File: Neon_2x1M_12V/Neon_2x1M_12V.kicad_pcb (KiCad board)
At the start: 2 copper layers, 77.5 x 51.5 mm, 47 parts, among them J2 Barrel_Jack_MountingPin, J4 Barrel_Jack_MountingPin, J5 Barrel_Jack_MountingPin, J6 Conn_01x03_Pin, Q1 IRLML2502TRPBF, Q2 IRLML2502TRPBF, Q3 BSS138, Q4 BSS138, Q5 BSS138, SW1 SW_Push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

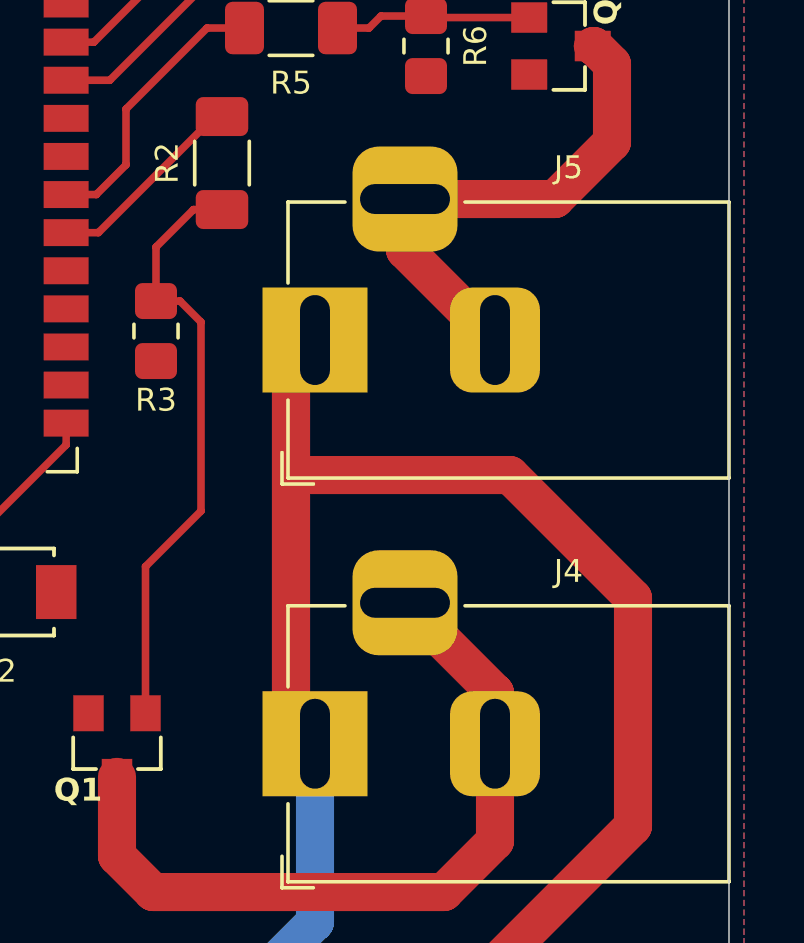
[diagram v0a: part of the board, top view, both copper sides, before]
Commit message: updated output jack routing
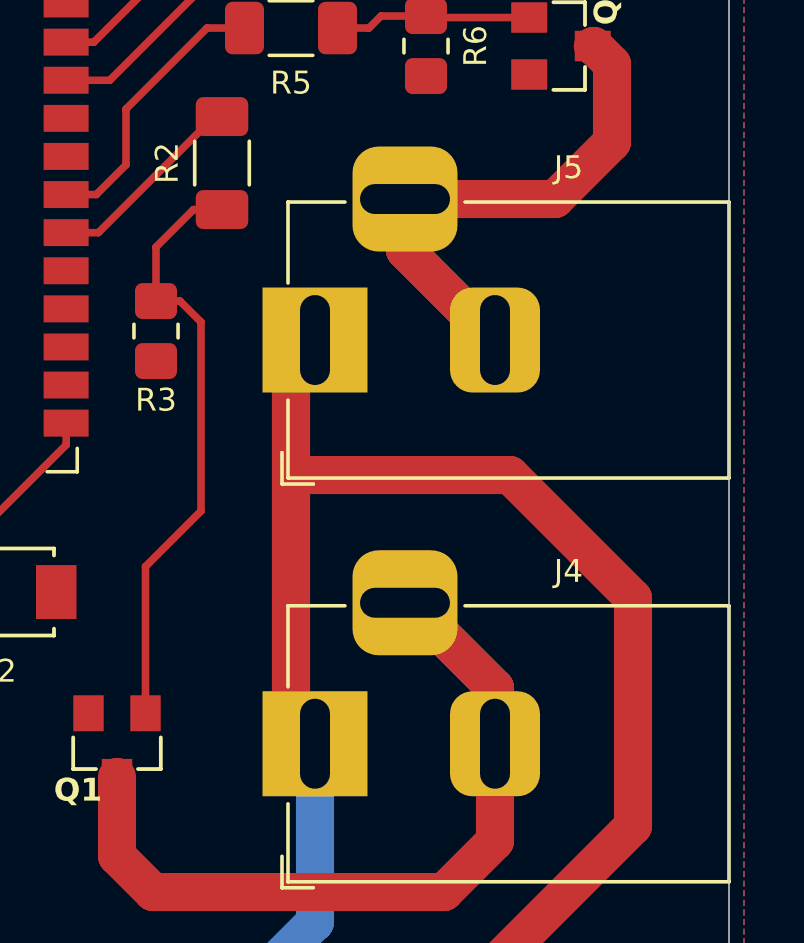
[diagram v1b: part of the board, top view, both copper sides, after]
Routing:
- net B_Jack: track 25.6 -> 31.8 mm
- net P_Jack: track 17.1 -> 23.1 mm
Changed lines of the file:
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@@
 	)
 	(segment
-		(start 167.3 69.7)
-		(end 166.1 68.5)
+		(start 178.7 64.7575)
+		(end 178.7 62.9)
 		(width 1.27)
 		(layer "F.Cu")
@@
 	)
 	(segment
-		(start 178.7 64.7575)
-		(end 178.7 63.0575)
+		(start 167.3 69.7)
+		(end 166.1 68.5)
 		(width 1.27)
 		(layer "F.Cu")
@@
 	)
 	(segment
-		(start 178.7 63.0575)
+		(start 178.7 62.9)
+		(end 175.8575 60.0575)
+		(width 1.27)
+		(layer "F.Cu")
+		(net 37)
+	)
+	(segment
+		(start 175.8575 60.0575)
 		(end 175.7 60.0575)
 		(width 1.27)
@@
 		(width 1.27)
 		(layer "F.Cu")
+		(net 37)
+	)
+	(segment
+		(start 175.8575 60.0575)
+		(end 178.7 62.9)
+		(width 1.27)
+		(layer "B.Cu")
+		(net 37)
+	)
+	(segment
+		(start 178.7 62.9)
+		(end 178.7 64.7575)
+		(width 1.27)
+		(layer "B.Cu")
+		(net 37)
+	)
+	(segment
+		(start 175.7 60.0575)
+		(end 175.8575 60.0575)
+		(width 1.27)
+		(layer "B.Cu")
 		(net 37)
 	)
@@
 		(net 38)
 	)
+	(segment
+		(start 175.7 46.6)
+		(end 175.7 48.3)
+		(width 1.27)
+		(layer "B.Cu")
+		(net 38)
+	)
+	(segment
+		(start 175.7 48.3)
+		(end 178.7 51.3)
+		(width 1.27)
+		(layer "B.Cu")
+		(net 38)
+	)

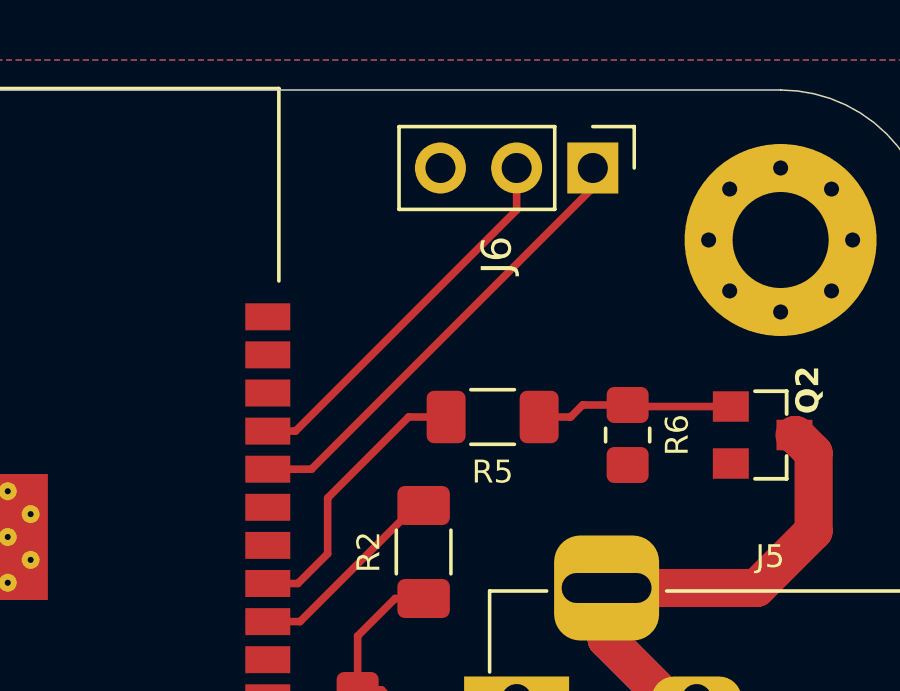
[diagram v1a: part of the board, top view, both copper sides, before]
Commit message: updated JST PIN header placement
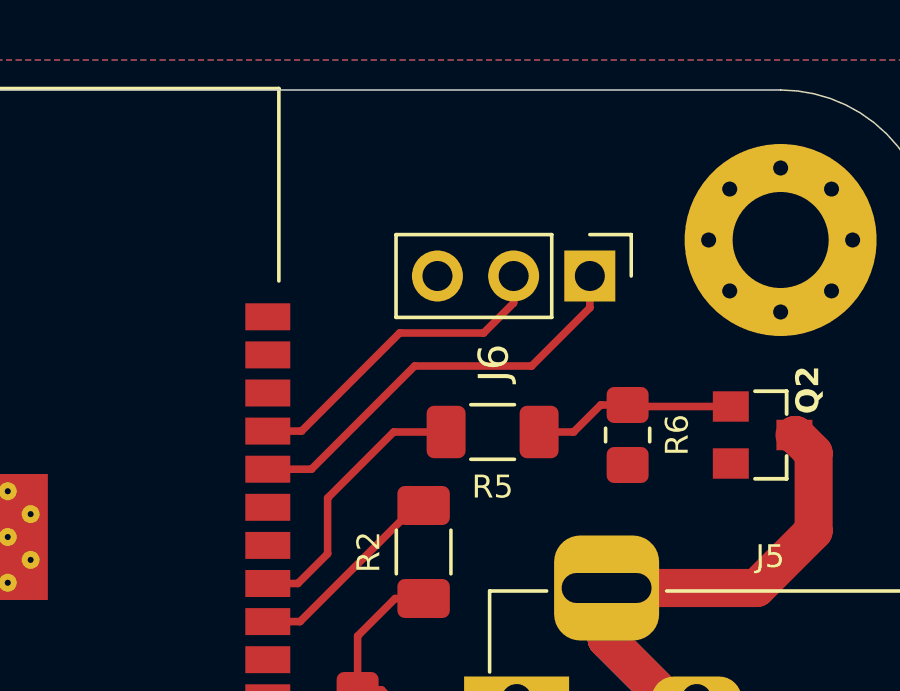
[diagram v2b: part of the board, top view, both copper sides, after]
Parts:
- moved J6 3.60 mm to (175.1, 36.2)
- moved R5 0.50 mm to (171.9, 41.4)
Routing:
- net ESP_U0TX: track 12.7 -> 10.9 mm
- net ESP_U0RX: track 15.4 -> 14.0 mm
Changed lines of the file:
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@@
 	(footprint "Connector_PinHeader_2.54mm:PinHeader_1x03_P2.54mm_Vertical"
 		(layer "F.Cu")
-		(at 175.24 32.6 -90)
+		(at 175.14 36.2 -90)
 		(descr "Through hole straight pin header, 1x03, 2.54mm pitch, single row")
 		(tags "Through hole pin header THT 1x03 2.54mm single row")
@@
 	(footprint "Resistor_SMD:R_1206_3216Metric_Pad1.30x1.75mm_HandSolder"
 		(layer "F.Cu")
-		(at 171.9 40.9 180)
+		(at 171.9 41.4 180)
 		(descr "Resistor SMD 1206 (3216 Metric), square (rectangular) end terminal, IPC-7351 nominal with elongated pad for handsoldering. (Body size source: IPC-SM-782 page 72, https://www.pcb-3d.com/wordpress/wp-content/uploads/ipc-sm-782a_amendment_1_and_2.pdf), generated with kicad-footprint-generator")
 		(tags "resistor handsolder")
@@
 	)
 	(segment
-		(start 165.33 41.37)
-		(end 164.405 41.37)
+		(start 171.6 38.1)
+		(end 172.6 37.1)
 		(width 0.254)
 		(layer "F.Cu")
@@
 	)
 	(segment
-		(start 172.7 32.6)
-		(end 172.7 34)
+		(start 168.8 38.1)
+		(end 171.6 38.1)
 		(width 0.254)
 		(layer "F.Cu")
@@
 	)
 	(segment
-		(start 172.7 34)
-		(end 165.33 41.37)
+		(start 172.6 37.1)
+		(end 172.6 36.2)
+		(width 0.254)
+		(layer "F.Cu")
+		(net 26)
+	)
+	(segment
+		(start 164.405 41.37)
+		(end 165.53 41.37)
+		(width 0.254)
+		(layer "F.Cu")
+		(net 26)
+	)
+	(segment
+		(start 165.53 41.37)
+		(end 168.8 38.1)
 		(width 0.254)
 		(layer "F.Cu")
@@
 	)
 	(segment
-		(start 164.405 46.45)
-		(end 165.409 46.45)
+		(start 166.4 45.459)
+		(end 166.4 43.6)
 		(width 0.254)
 		(layer "F.Cu")
@@
 	)
 	(segment
-		(start 165.409 46.45)
-		(end 166.4 45.459)
+		(start 168.6 41.4)
+		(end 170.35 41.4)
 		(width 0.254)
 		(layer "F.Cu")
@@
 	)
 	(segment
-		(start 166.4 45.459)
-		(end 166.4 43.6)
+		(start 166.4 43.6)
+		(end 168.6 41.4)
 		(width 0.254)
 		(layer "F.Cu")
@@
 	)
 	(segment
-		(start 166.4 43.6)
-		(end 169.1 40.9)
+		(start 164.405 46.45)
+		(end 165.409 46.45)
 		(width 0.254)
 		(layer "F.Cu")
@@
 	)
 	(segment
-		(start 169.1 40.9)
-		(end 169.95 40.9)
+		(start 165.409 46.45)
+		(end 166.4 45.459)
 		(width 0.254)
 		(layer "F.Cu")
@@
 	)
 	(segment
+		(start 169.3 39.2)
+		(end 165.86 42.64)
+		(width 0.254)
+		(layer "F.Cu")
+		(net 36)
+	)
+	(segment
+		(start 175.14 37.26)
+		(end 173.2 39.2)
+		(width 0.254)
+		(layer "F.Cu")
+		(net 36)
+	)
+	(segment
 		(start 165.86 42.64)
 		(end 164.405 42.64)
@@
 	)
 	(segment
-		(start 175.24 33.26)
-		(end 165.86 42.64)
+		(start 173.2 39.2)
+		(end 169.3 39.2)
 		(width 0.254)
 		(layer "F.Cu")
@@
 	)
 	(segment
-		(start 175.24 32.6)
-		(end 175.24 33.26)
+		(start 175.14 36.2)
+		(end 175.14 37.26)
 		(width 0.254)
 		(layer "F.Cu")
@@
 	)
 	(segment
-		(start 174.9 40.5)
-		(end 176.4 40.5)
+		(start 174.6 41.4)
+		(end 175.5 40.5)
 		(width 0.254)
 		(layer "F.Cu")
@@
 	)
 	(segment
-		(start 174.5 40.9)
-		(end 174.9 40.5)
+		(start 176.45 40.55)
+		(end 176.4 40.5)
 		(width 0.254)
 		(layer "F.Cu")
@@
 	)
 	(segment
-		(start 173.45 40.9)
-		(end 174.5 40.9)
+		(start 175.5 40.5)
+		(end 176.4 40.5)
 		(width 0.254)
 		(layer "F.Cu")
@@
 	)
 	(segment
-		(start 176.45 40.55)
-		(end 176.4 40.5)
+		(start 173.45 41.4)
+		(end 174.6 41.4)
 		(width 0.254)
 		(layer "F.Cu")
